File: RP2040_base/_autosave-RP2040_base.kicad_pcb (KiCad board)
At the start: 4 copper layers, 94.4 x 72.8 mm, 126 parts, among them J1 CPU1 USB, J16 Conn_02x05_Odd_Even, J18 Conn_01x06, J19 Conn_02x05_Odd_Even, J20 Conn_02x05_Odd_Even, J21 Conn_01x06, J3 Encoder 1, J5 Conn_01x06, J7 Conn_02x05_Odd_Even, Q3 NCE40P05Y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

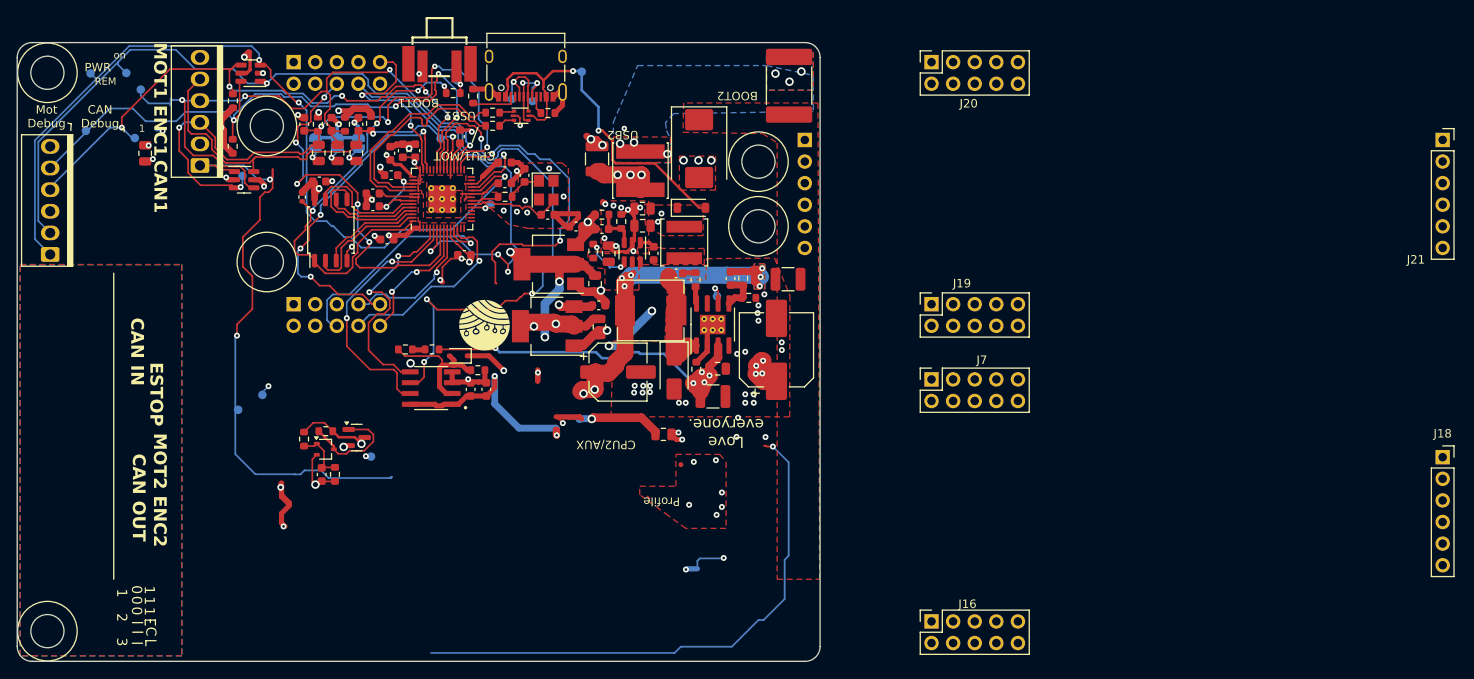
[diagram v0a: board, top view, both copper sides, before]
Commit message: Remove 2nd Motor Stuff.
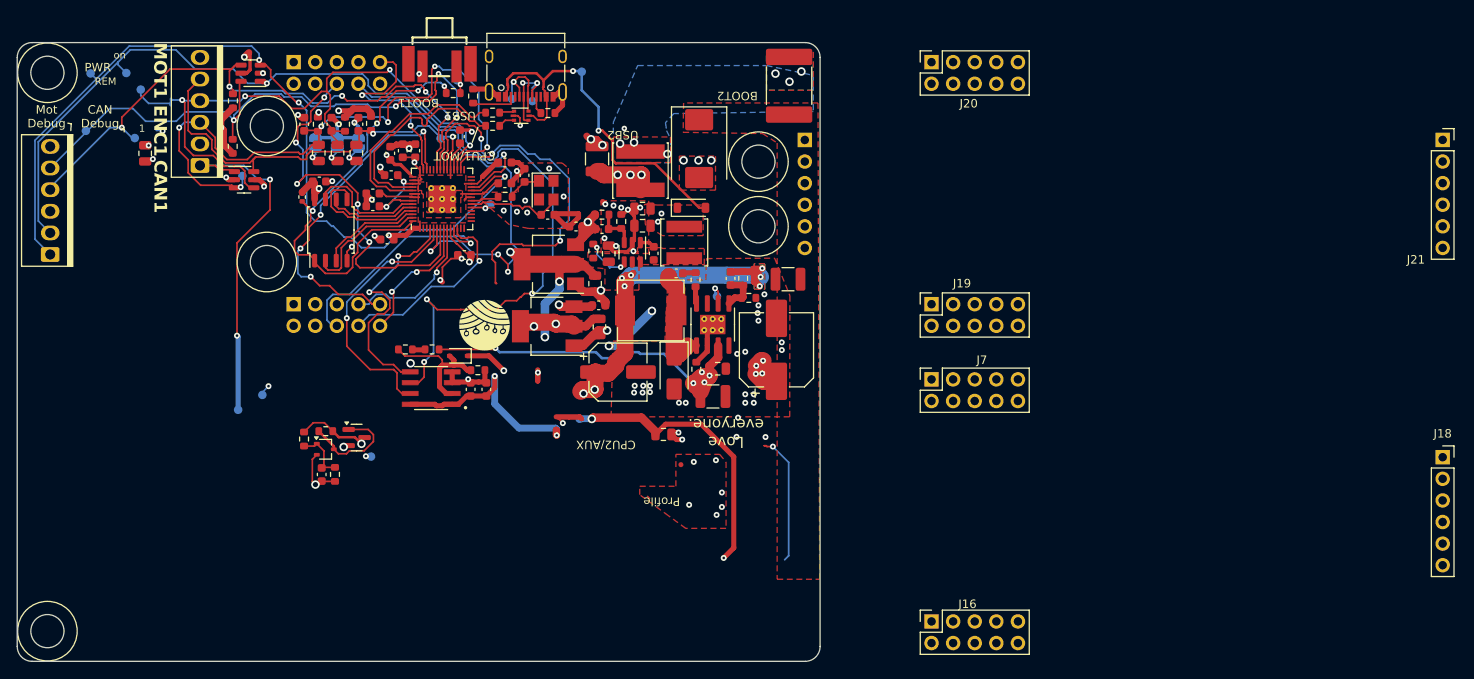
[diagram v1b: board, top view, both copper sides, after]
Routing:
- net +3V3: track 363.5 -> 270.1 mm, vias 18 -> 15
- net M2B_PWM_H: track 64.1 -> 0.00 mm, vias 1 -> 0
- net +12V: track 121.8 -> 84.0 mm
- net /TH_MOTOR1: track 71.3 -> 42.3 mm
- net (no net): track 0.00 -> 15.3 mm, vias 0 -> 1
- removed copper zone on B.Cu, net (none)
- removed copper zone on F.Cu, net (none)
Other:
- board text removed: "0"
- board text removed: "2"
- board text removed: "C"
- board text removed: "CAN IN"
- board text removed: "CAN OUT"
- board text removed: "ESTOP"
- board text removed: "MOT2 ENC2"
